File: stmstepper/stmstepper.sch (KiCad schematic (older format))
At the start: 19 parts, among them J1 Conn_02x12_Odd_Even, J2 Conn_02x12_Odd_Even, J3 Conn_02x12_Odd_Even, J4 Conn_02x12_Odd_Even, J5 CONN_01X08, J6 CONN_01X08, J7 CONN_01X08, J8 CONN_01X08, P1 CONN_01X02, P2 CONN_01X04, P3 CONN_01X04, P4 CONN_01X05, P5 CONN_01X05, P6 CONN_01X03, U1 SN65HVD230, U2 7805

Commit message: add stmstepper pcb
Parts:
- removed P6: CONN_01X03, symbol CONN_01X03
- added P6: Conn_02x03_Odd_Even, symbol Conn_02x03_Odd_Even
- J5, J6, J7, J8: footprint Socket_Strips:Socket_Strip_Angled_1x08_Pitch2.54mm -> Socket_Strips:Socket_Strip_Straight_1x08_Pitch2.54mm
- R1: footprint (none) -> Resistors_SMD:R_0805_HandSoldering
- U2: footprint (none) -> TO_SOT_Packages_THT:TO-220_Horizontal; symbol 7805 -> LM7805
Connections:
- wire segments 202 -> 212
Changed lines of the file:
@@
 LIBS:valves
 LIBS:stm32
-LIBS:sn65hvd230
 LIBS:stmstepper-cache
 EELAYER 25 0
@@
 UART1_TX
 $Comp
-L GND #PWR01
+L GND #PWR6
 U 1 1 5A41FDCF
 P 4500 2000
-F 0 "#PWR01" H 4500 1750 50  0001 C CNN
+F 0 "#PWR6" H 4500 1750 50  0001 C CNN
 F 1 "GND" H 4500 1850 50  0000 C CNN
 F 2 "" H 4500 2000 50  0001 C CNN
@@
 TIM1_CH1N
 $Comp
-L GND #PWR02
+L GND #PWR14
 U 1 1 5A422E36
 P 9600 2000
-F 0 "#PWR02" H 9600 1750 50  0001 C CNN
+F 0 "#PWR14" H 9600 1750 50  0001 C CNN
 F 1 "GND" H 9600 1850 50  0000 C CNN
 F 2 "" H 9600 2000 50  0001 C CNN
@@
 TIM8_CH4
 $Comp
-L GND #PWR03
+L GND #PWR9
 U 1 1 5A4240DB
 P 7000 2000
-F 0 "#PWR03" H 7000 1750 50  0001 C CNN
+F 0 "#PWR9" H 7000 1750 50  0001 C CNN
 F 1 "GND" H 7000 1850 50  0000 C CNN
 F 2 "" H 7000 2000 50  0001 C CNN
@@
 TIM4_CH1
 $Comp
-L GND #PWR04
+L GND #PWR18
 U 1 1 5A42436F
 P 12100 2000
-F 0 "#PWR04" H 12100 1750 50  0001 C CNN
+F 0 "#PWR18" H 12100 1750 50  0001 C CNN
 F 1 "GND" H 12100 1850 50  0000 C CNN
 F 2 "" H 12100 2000 50  0001 C CNN
@@
 	7000 2850 6100 2850
 $Comp
-L GND #PWR05
+L GND #PWR8
 U 1 1 5A448572
 P 4700 3100
-F 0 "#PWR05" H 4700 2850 50  0001 C CNN
+F 0 "#PWR8" H 4700 2850 50  0001 C CNN
 F 1 "GND" H 4700 2950 50  0000 C CNN
 F 2 "" H 4700 3100 50  0001 C CNN
@@
 $EndComp
 $Comp
-L GND #PWR06
+L GND #PWR10
 U 1 1 5A4485F8
 P 7000 3100
-F 0 "#PWR06" H 7000 2850 50  0001 C CNN
+F 0 "#PWR10" H 7000 2850 50  0001 C CNN
 F 1 "GND" H 7000 2950 50  0000 C CNN
 F 2 "" H 7000 3100 50  0001 C CNN
@@
 	12100 2850 12100 3100
 $Comp
-L GND #PWR07
+L GND #PWR19
 U 1 1 5A453321
 P 12100 3100
-F 0 "#PWR07" H 12100 2850 50  0001 C CNN
+F 0 "#PWR19" H 12100 2850 50  0001 C CNN
 F 1 "GND" H 12100 2950 50  0000 C CNN
 F 2 "" H 12100 3100 50  0001 C CNN
@@
 	9600 2850 9600 3100
 $Comp
-L GND #PWR08
+L GND #PWR15
 U 1 1 5A453473
 P 9600 3100
-F 0 "#PWR08" H 9600 2850 50  0001 C CNN
+F 0 "#PWR15" H 9600 2850 50  0001 C CNN
 F 1 "GND" H 9600 2950 50  0000 C CNN
 F 2 "" H 9600 3100 50  0001 C CNN
@@
 	4500 2850 4500 3100
 $Comp
-L GND #PWR09
+L GND #PWR7
 U 1 1 5A45354A
 P 4500 3100
-F 0 "#PWR09" H 4500 2850 50  0001 C CNN
+F 0 "#PWR7" H 4500 2850 50  0001 C CNN
 F 1 "GND" H 4500 2950 50  0000 C CNN
 F 2 "" H 4500 3100 50  0001 C CNN
@@
 Connection ~ 7000 2850
 $Comp
-L GND #PWR010
+L GND #PWR1
 U 1 1 5A475CC8
 P 2400 3050
-F 0 "#PWR010" H 2400 2800 50  0001 C CNN
+F 0 "#PWR1" H 2400 2800 50  0001 C CNN
 F 1 "GND" H 2400 2900 50  0000 C CNN
 F 2 "" H 2400 3050 50  0001 C CNN
@@
 F 0 "J7" H 1800 8050 50  0000 C CNN
 F 1 "CONN_01X08" V 1900 7600 50  0000 C CNN
-F 2 "Socket_Strips:Socket_Strip_Angled_1x08_Pitch2.54mm" H 1800 7600 50  0001 C CNN
+F 2 "Socket_Strips:Socket_Strip_Straight_1x08_Pitch2.54mm" H 1800 7600 50  0001 C CNN
 F 3 "" H 1800 7600 50  0000 C CNN
 	1    1800 7600
@@
 F 0 "J8" H 1800 9300 50  0000 C CNN
 F 1 "CONN_01X08" V 1900 8850 50  0000 C CNN
-F 2 "Socket_Strips:Socket_Strip_Angled_1x08_Pitch2.54mm" H 1800 8850 50  0001 C CNN
+F 2 "Socket_Strips:Socket_Strip_Straight_1x08_Pitch2.54mm" H 1800 8850 50  0001 C CNN
 F 3 "" H 1800 8850 50  0000 C CNN
 	1    1800 8850
@@
 B-2B
 $Comp
-L GND #PWR011
+L GND #PWR4
 U 1 1 5A94A966
 P 2900 7450
-F 0 "#PWR011" H 2900 7200 50  0001 C CNN
+F 0 "#PWR4" H 2900 7200 50  0001 C CNN
 F 1 "GND" H 2900 7300 50  0000 C CNN
 F 2 "" H 2900 7450 50  0001 C CNN
@@
 $EndComp
 $Comp
-L GND #PWR012
+L GND #PWR5
 U 1 1 5A94A995
 P 2900 8050
-F 0 "#PWR012" H 2900 7800 50  0001 C CNN
+F 0 "#PWR5" H 2900 7800 50  0001 C CNN
 F 1 "GND" H 2900 7900 50  0000 C CNN
 F 2 "" H 2900 8050 50  0001 C CNN
@@
 	7700 8700 8250 8700
 $Comp
-L GND #PWR013
+L GND #PWR13
 U 1 1 5A94BD29
 P 8250 9000
-F 0 "#PWR013" H 8250 8750 50  0001 C CNN
+F 0 "#PWR13" H 8250 8750 50  0001 C CNN
 F 1 "GND" H 8250 8850 50  0000 C CNN
 F 2 "" H 8250 9000 50  0001 C CNN
@@
 F 0 "J5" H 1800 5500 50  0000 C CNN
 F 1 "CONN_01X08" V 1900 5050 50  0000 C CNN
-F 2 "Socket_Strips:Socket_Strip_Angled_1x08_Pitch2.54mm" H 1800 5050 50  0001 C CNN
+F 2 "Socket_Strips:Socket_Strip_Straight_1x08_Pitch2.54mm" H 1800 5050 50  0001 C CNN
 F 3 "" H 1800 5050 50  0000 C CNN
 	1    1800 5050
@@
 F 0 "J6" H 1800 6750 50  0000 C CNN
 F 1 "CONN_01X08" V 1900 6300 50  0000 C CNN
-F 2 "Socket_Strips:Socket_Strip_Angled_1x08_Pitch2.54mm" H 1800 6300 50  0001 C CNN
+F 2 "Socket_Strips:Socket_Strip_Straight_1x08_Pitch2.54mm" H 1800 6300 50  0001 C CNN
 F 3 "" H 1800 6300 50  0000 C CNN
 	1    1800 6300
@@
 A-2B
 $Comp
-L GND #PWR014
+L GND #PWR2
 U 1 1 5A94C348
 P 2900 4900
-F 0 "#PWR014" H 2900 4650 50  0001 C CNN
+F 0 "#PWR2" H 2900 4650 50  0001 C CNN
 F 1 "GND" H 2900 4750 50  0000 C CNN
 F 2 "" H 2900 4900 50  0001 C CNN
@@
 $EndComp
 $Comp
-L GND #PWR015
+L GND #PWR3
 U 1 1 5A94C34E
 P 2900 5500
-F 0 "#PWR015" H 2900 5250 50  0001 C CNN
+F 0 "#PWR3" H 2900 5250 50  0001 C CNN
 F 1 "GND" H 2900 5350 50  0000 C CNN
 F 2 "" H 2900 5500 50  0001 C CNN
@@
 Text Notes 900  6400 0    157  ~ 31
 J6-A
-$Comp
-L SN65HVD230 U1
-U 1 1 5A94D65D
-P 12050 7250
-F 0 "U1" H 11950 7650 50  0000 R CNN
-F 1 "SN65HVD230" H 11950 7550 50  0000 R CNN
-F 2 "Housings_SOIC:SOIC-8_3.9x4.9mm_Pitch1.27mm" H 12050 6750 50  0001 C CNN
-F 3 "" H 11950 7650 50  0001 C CNN
-	1    12050 7250
-	1    0    0    -1
-$EndComp
 Text Notes 10400 6450 0    197  ~ 39
 CAN
@@
 +3V3
 $Comp
-L GND #PWR016
+L GND #PWR17
 U 1 1 5A94E2DA
 P 12050 7850
-F 0 "#PWR016" H 12050 7600 50  0001 C CNN
+F 0 "#PWR17" H 12050 7600 50  0001 C CNN
 F 1 "GND" H 12050 7700 50  0000 C CNN
 F 2 "" H 12050 7850 50  0001 C CNN
@@
 F 0 "R1" V 12880 7550 50  0000 C CNN
 F 1 "R120" V 12800 7550 50  0000 C CNN
-F 2 "" V 12730 7550 50  0001 C CNN
+F 2 "Resistors_SMD:R_0805_HandSoldering" V 12730 7550 50  0001 C CNN
 F 3 "" H 12800 7550 50  0000 C CNN
 	1    12800 7550
 	1    0    0    -1
 $EndComp
-$Comp
-L CONN_01X03 P6
-U 1 1 5A94E6A1
-P 14250 7200
-F 0 "P6" H 14250 7400 50  0000 C CNN
-F 1 "CONN_01X03" V 14350 7200 50  0000 C CNN
-F 2 "" H 14250 7200 50  0001 C CNN
-F 3 "" H 14250 7200 50  0000 C CNN
-	1    14250 7200
-	1    0    0    -1
-$EndComp
 Wire Wire Line
 	13050 7100 14050 7100
@@
 Connection ~ 12800 7700
 $Comp
-L GND #PWR017
+L GND #PWR20
 U 1 1 5A94F0CE
 P 13700 7500
-F 0 "#PWR017" H 13700 7250 50  0001 C CNN
+F 0 "#PWR20" H 13700 7250 50  0001 C CNN
 F 1 "GND" H 13700 7350 50  0000 C CNN
 F 2 "" H 13700 7500 50  0001 C CNN
@@
 VIN
 $Comp
-L 7805 U2
+L LM7805 U2
 U 1 1 5A94F7CA
 P 12050 4800
 F 0 "U2" H 12200 4604 50  0000 C CNN
 F 1 "7805" H 12050 5000 50  0000 C CNN
-F 2 "" H 12050 4800 50  0001 C CNN
+F 2 "TO_SOT_Packages_THT:TO-220_Horizontal" H 12050 4800 50  0001 C CNN
 F 3 "" H 12050 4800 50  0000 C CNN
 	1    12050 4800
@@
 	12450 4750 12800 4750
 $Comp
-L GND #PWR018
+L GND #PWR16
 U 1 1 5A9500FA
 P 12050 5200
-F 0 "#PWR018" H 12050 4950 50  0001 C CNN
+F 0 "#PWR16" H 12050 4950 50  0001 C CNN
 F 1 "GND" H 12050 5050 50  0000 C CNN
 F 2 "" H 12050 5200 50  0001 C CNN
@@
 GPIO0
 $Comp
-L GND #PWR019
+L GND #PWR12
 U 1 1 5A954F8D
 P 7700 6100
-F 0 "#PWR019" H 7700 5850 50  0001 C CNN
+F 0 "#PWR12" H 7700 5850 50  0001 C CNN
 F 1 "GND" H 7700 5950 50  0000 C CNN
 F 2 "" H 7700 6100 50  0001 C CNN
@@
 $EndComp
 $Comp
-L GND #PWR020
+L GND #PWR11
 U 1 1 5A954FC8
 P 7700 5300
-F 0 "#PWR020" H 7700 5050 50  0001 C CNN
+F 0 "#PWR11" H 7700 5050 50  0001 C CNN
 F 1 "GND" H 7700 5150 50  0000 C CNN
 F 2 "" H 7700 5300 50  0001 C CNN
@@
 	7700 6100 8100 6100
 $Comp
-L PWR_FLAG #FLG021
+L PWR_FLAG #FLG1
 U 1 1 5A95E68F
 P 7850 8600
-F 0 "#FLG021" H 7850 8695 50  0001 C CNN
+F 0 "#FLG1" H 7850 8695 50  0001 C CNN
 F 1 "PWR_FLAG" H 7850 8780 50  0000 C CNN
 F 2 "" H 7850 8600 50  0000 C CNN
@@
 Connection ~ 7850 8700
 $Comp
-L PWR_FLAG #FLG022
+L PWR_FLAG #FLG2
 U 1 1 5A95E7BD
 P 7850 8950
-F 0 "#FLG022" H 7850 9045 50  0001 C CNN
+F 0 "#FLG2" H 7850 9045 50  0001 C CNN
 F 1 "PWR_FLAG" H 7850 9130 50  0000 C CNN
 F 2 "" H 7850 8950 50  0000 C CNN
@@
 	12050 6600 12050 6950
 $Comp
-L PWR_FLAG #FLG023
+L PWR_FLAG #FLG3
 U 1 1 5A95EF58
 P 8100 6800
-F 0 "#FLG023" H 8100 6895 50  0001 C CNN
+F 0 "#FLG3" H 8100 6895 50  0001 C CNN
 F 1 "PWR_FLAG" H 8100 6980 50  0000 C CNN
 F 2 "" H 8100 6800 50  0000 C CNN
@@
 	8100 6800 8100 7000
 Connection ~ 8100 7000
+$Comp
+L SN65HVD230 U1
+U 1 1 5A95D6AB
+P 12050 7250
+F 0 "U1" H 11950 7650 50  0000 R CNN
+F 1 "SN65HVD230" H 11950 7550 50  0000 R CNN
+F 2 "Housings_SOIC:SOIC-8_3.9x4.9mm_Pitch1.27mm" H 12050 6750 50  0001 C CNN
+F 3 "" H 11950 7650 50  0001 C CNN
+	1    12050 7250
+	1    0    0    -1
+$EndComp
+$Comp
+L Conn_02x03_Odd_Even P6
+U 1 1 5A95F795
+P 14250 7200
+F 0 "P6" H 14300 7400 50  0000 C CNN
+F 1 "Conn_02x03_Odd_Even" H 14300 7000 50  0000 C CNN
+F 2 "" H 14250 7200 50  0001 C CNN
+F 3 "" H 14250 7200 50  0001 C CNN
+	1    14250 7200
+	1    0    0    -1
+$EndComp
+Wire Wire Line
+	13750 7200 13750 6800
+Wire Wire Line
+	13750 6800 14650 6800
+Wire Wire Line
+	14650 6800 14650 7200
+Wire Wire Line
+	14650 7200 14550 7200
+Connection ~ 13750 7200
+Wire Wire Line
+	14550 7300 14750 7300
+Wire Wire Line
+	14750 7300 14750 7450
+Wire Wire Line
+	14750 7450 13700 7450
+Connection ~ 13700 7450
+Wire Wire Line
+	14550 7100 14550 6900
+Wire Wire Line
+	14550 6900 14000 6900
+Wire Wire Line
+	14000 6900 14000 7100
+Connection ~ 14000 7100
 $EndSCHEMATC

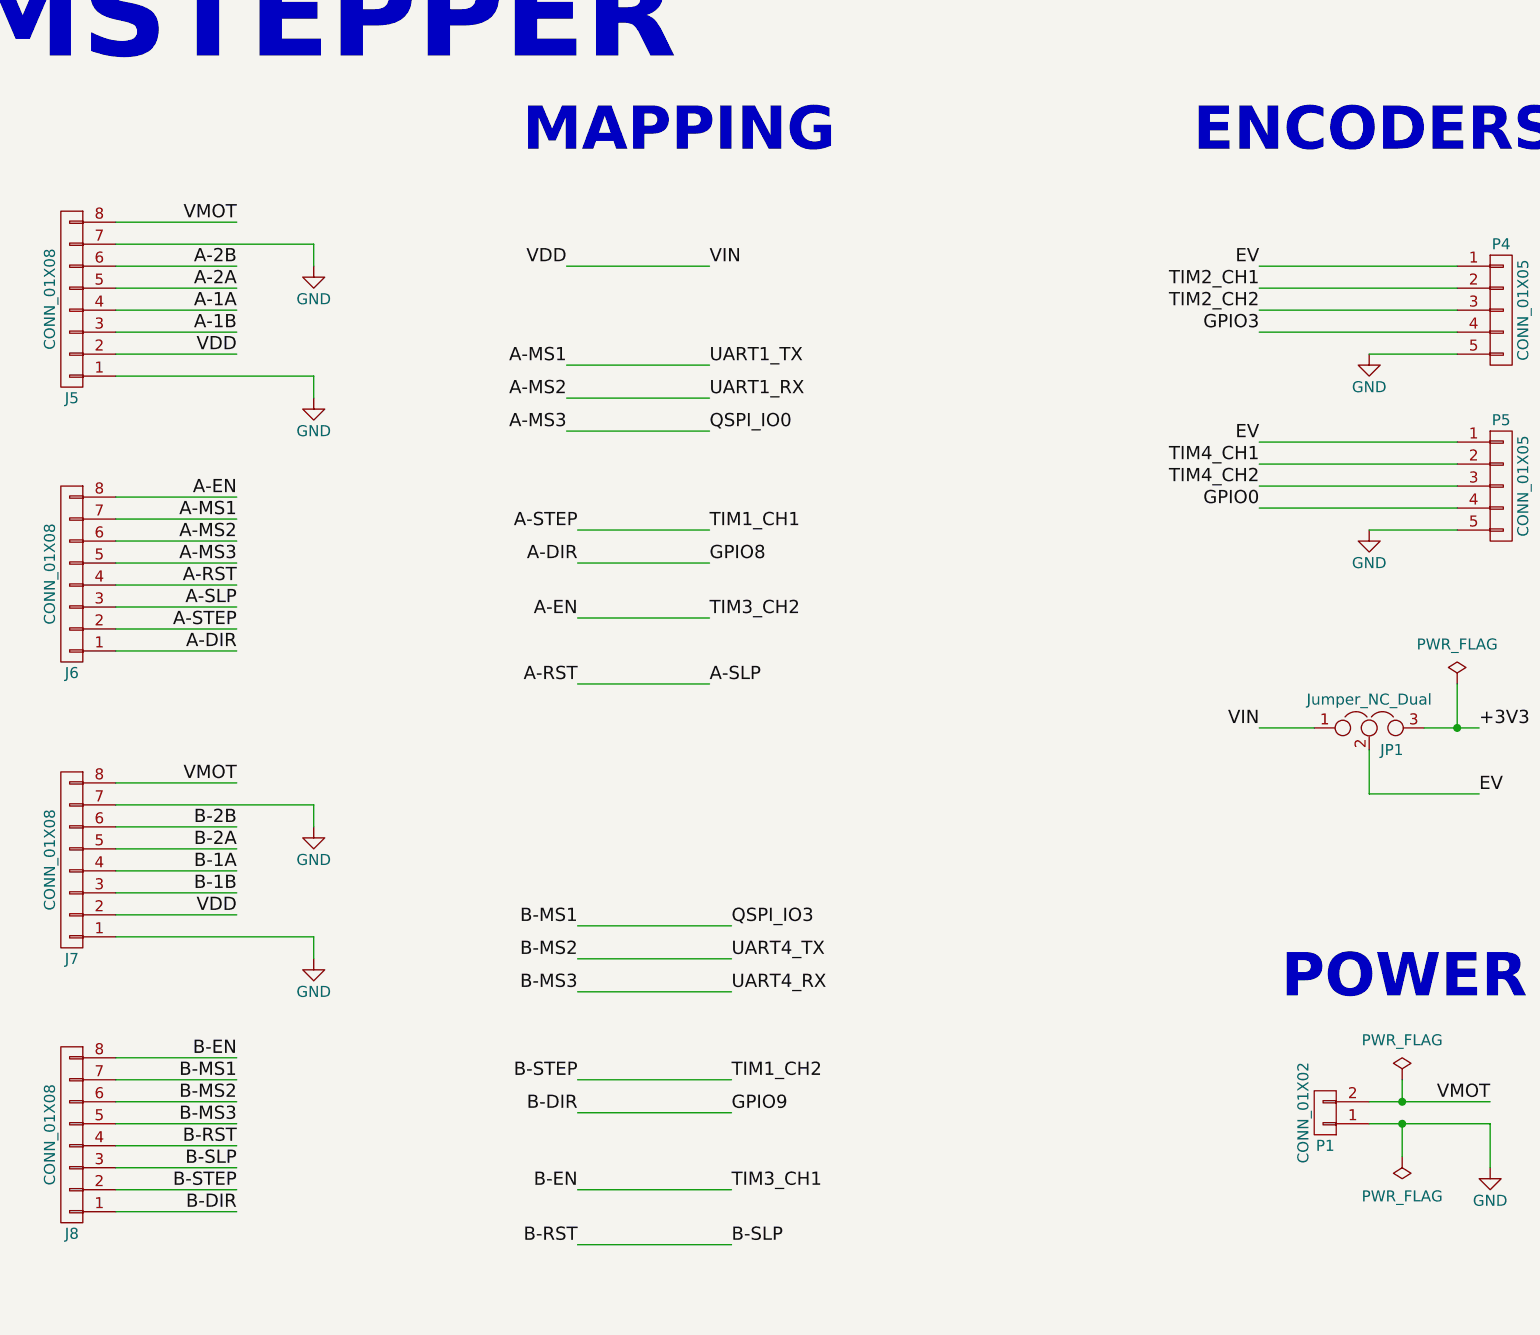
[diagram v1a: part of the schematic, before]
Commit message: final adjustments stmstepper, add logos
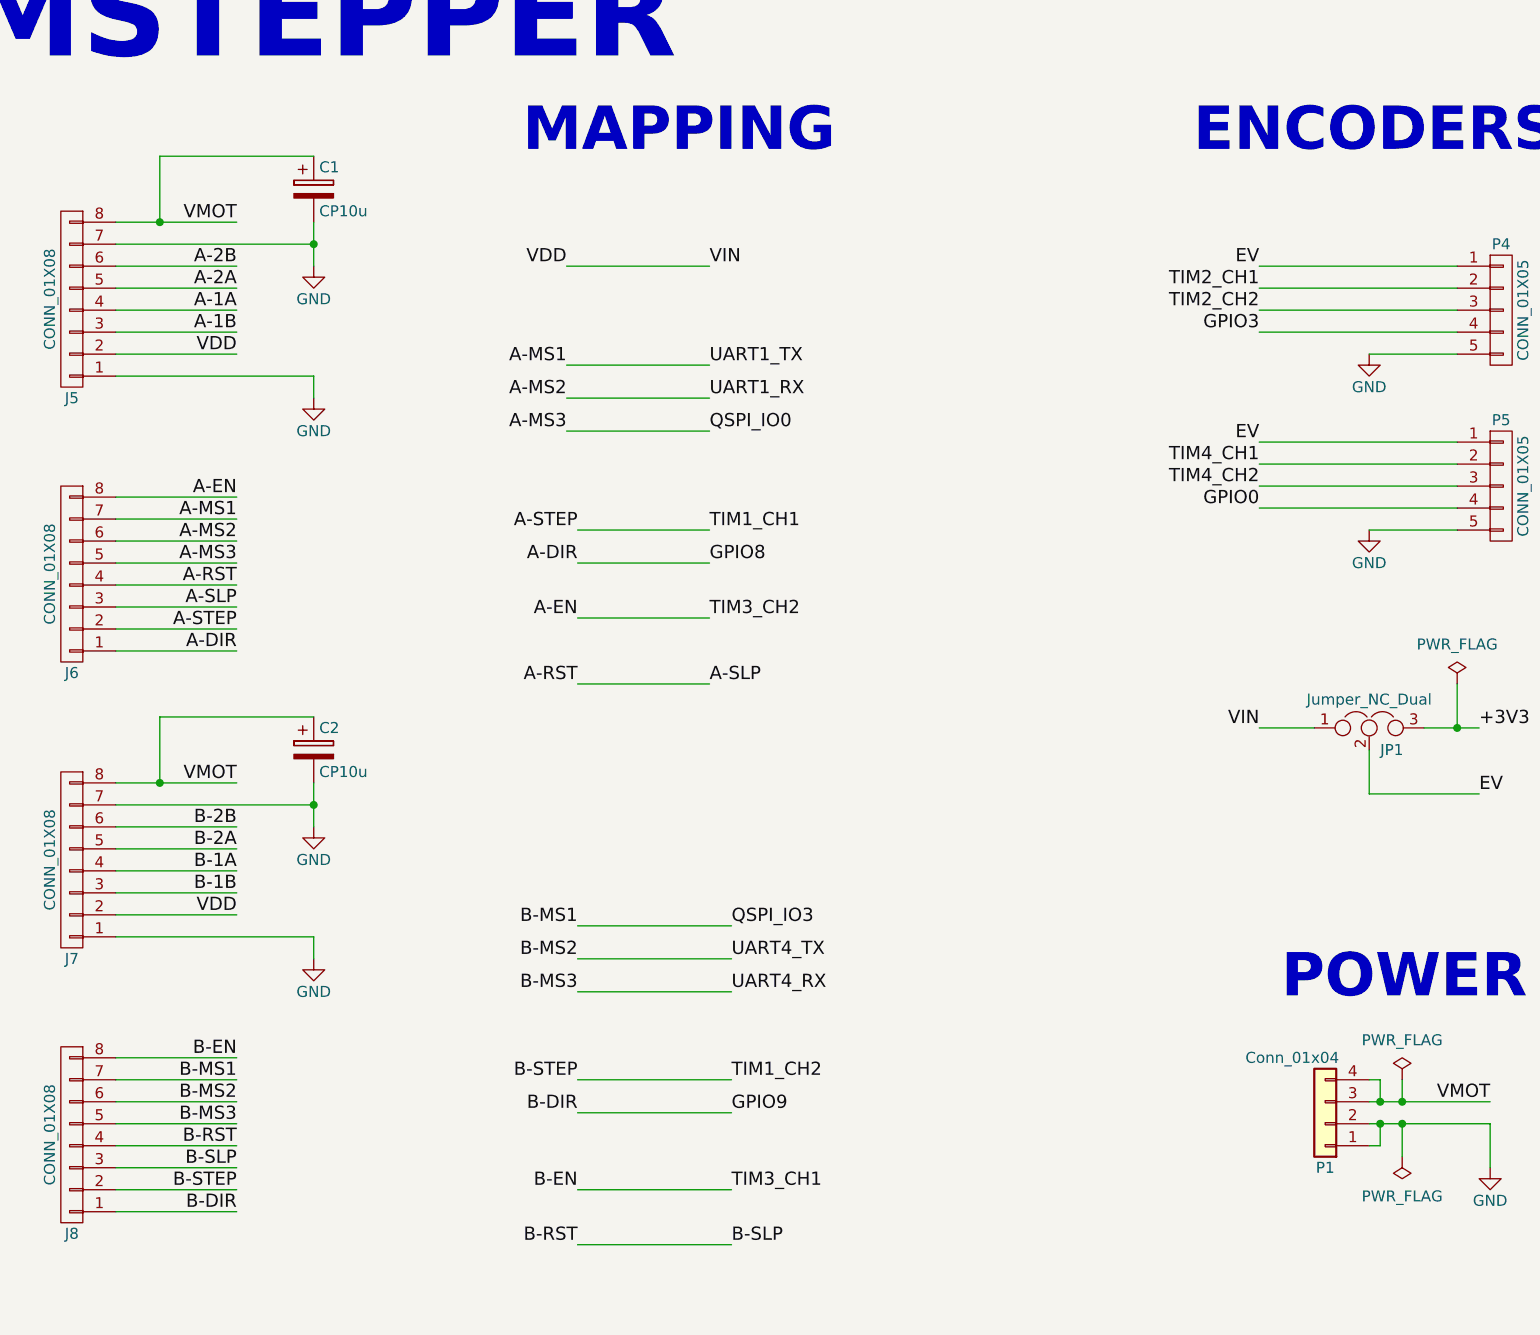
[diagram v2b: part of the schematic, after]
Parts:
- removed P1: CONN_01X02, Connectors:AK300-2, symbol CONN_01X02
- added C1, C2: CP10u, Capacitors_SMD:CP_Elec_8x6.7, symbol CP
- added P1: Conn_01x04, symbol Conn_01x04
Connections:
- wire segments 212 -> 220
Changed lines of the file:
@@
 	2000 7350 2900 7350
 Wire Wire Line
-	2900 7350 2900 7450
+	2900 7250 2900 7450
 Wire Wire Line
 	2000 7950 2900 7950
@@
 Text Notes 900  8950 0    157  ~ 31
 J8-B
-$Comp
-L CONN_01X02 P1
-U 1 1 5A94BB91
-P 7500 8750
-F 0 "P1" H 7500 8900 50  0000 C CNN
-F 1 "CONN_01X02" V 7600 8750 50  0000 C CNN
-F 2 "Connectors:AK300-2" H 7500 8750 50  0001 C CNN
-F 3 "" H 7500 8750 50  0000 C CNN
-	1    7500 8750
-	-1   0    0    1
-$EndComp
 Text Label 8250 8700 2    60   ~ 0
 VMOT
@@
 	2000 4800 2900 4800
 Wire Wire Line
-	2900 4800 2900 4900
+	2900 4700 2900 4900
 Wire Wire Line
 	2000 5400 2900 5400
@@
 	14000 6900 14000 7100
 Connection ~ 14000 7100
+$Comp
+L Conn_01x04 P1
+U 1 1 5A96F314
+P 7500 8800
+F 0 "P1" H 7500 9000 50  0000 C CNN
+F 1 "Conn_01x04" H 7650 8500 50  0000 C CNN
+F 2 "" H 7500 8800 50  0001 C CNN
+F 3 "" H 7500 8800 50  0001 C CNN
+	1    7500 8800
+	-1   0    0    1
+$EndComp
+Wire Wire Line
+	7750 8700 7750 8600
+Wire Wire Line
+	7750 8600 7700 8600
+Connection ~ 7750 8700
+Wire Wire Line
+	7750 8800 7750 8900
+Wire Wire Line
+	7750 8900 7700 8900
+Connection ~ 7750 8800
+$Comp
+L CP C1
+U 1 1 5A96FBDF
+P 2900 4550
+F 0 "C1" H 2925 4650 50  0000 L CNN
+F 1 "CP10u" H 2925 4450 50  0000 L CNN
+F 2 "Capacitors_SMD:CP_Elec_8x6.7" H 2938 4400 50  0001 C CNN
+F 3 "" H 2900 4550 50  0001 C CNN
+	1    2900 4550
+	1    0    0    -1
+$EndComp
+Wire Wire Line
+	2900 4400 2200 4400
+Wire Wire Line
+	2200 4400 2200 4700
+Connection ~ 2200 4700
+Connection ~ 2900 4800
+$Comp
+L CP C2
+U 1 1 5A96FFD3
+P 2900 7100
+F 0 "C2" H 2925 7200 50  0000 L CNN
+F 1 "CP10u" H 2925 7000 50  0000 L CNN
+F 2 "Capacitors_SMD:CP_Elec_8x6.7" H 2938 6950 50  0001 C CNN
+F 3 "" H 2900 7100 50  0001 C CNN
+	1    2900 7100
+	1    0    0    -1
+$EndComp
+Connection ~ 2900 7350
+Wire Wire Line
+	2900 6950 2200 6950
+Wire Wire Line
+	2200 6950 2200 7250
+Connection ~ 2200 7250
 $EndSCHEMATC
